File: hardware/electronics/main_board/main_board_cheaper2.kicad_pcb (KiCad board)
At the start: 2 copper layers, 125.5 x 125.5 mm, 144 parts, among them J1 TF-15X15, J2 RJ45, J3 Conn_02x04_Odd_Even, Q1 CSD18537NQ5A, Q2 CSD18537NQ5A, Q3 CSD18537NQ5A, Q4 CSD18537NQ5A, Q5 CSD18537NQ5A, Q6 CSD18537NQ5A, Q7 CSD18537NQ5A, Q8 CSD18537NQ5A, U1 P82B96

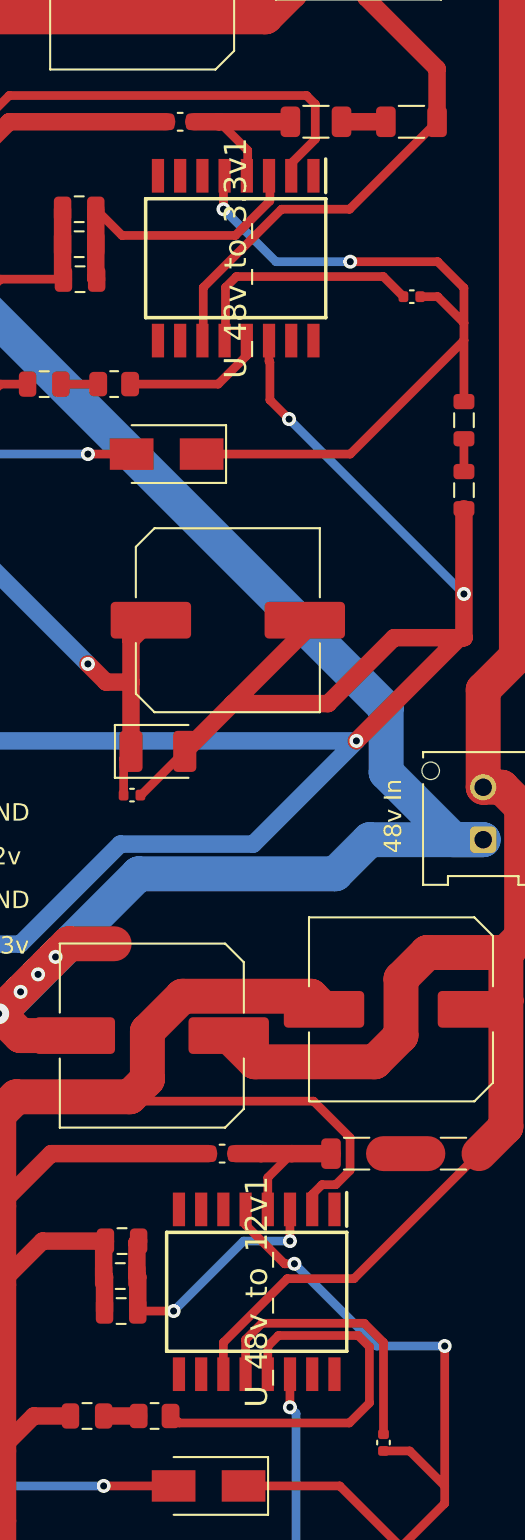
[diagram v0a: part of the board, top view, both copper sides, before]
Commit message: updated footprint to generic SOIC-16w so tooling rotates it properly."
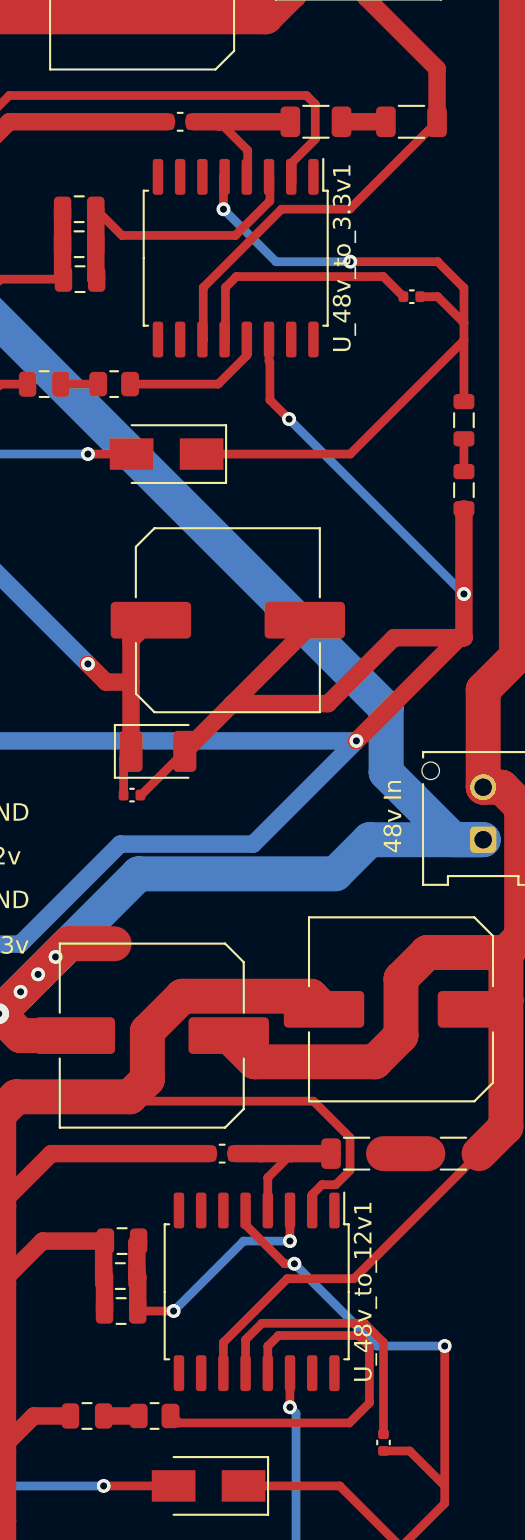
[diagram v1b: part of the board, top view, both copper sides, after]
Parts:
- U_48v_to_12v1, U_48v_to_3.3v1: footprint main_board:SOIC127P1032X265-16N -> Package_SO:SOIC-16W_7.5x10.3mm_P1.27mm

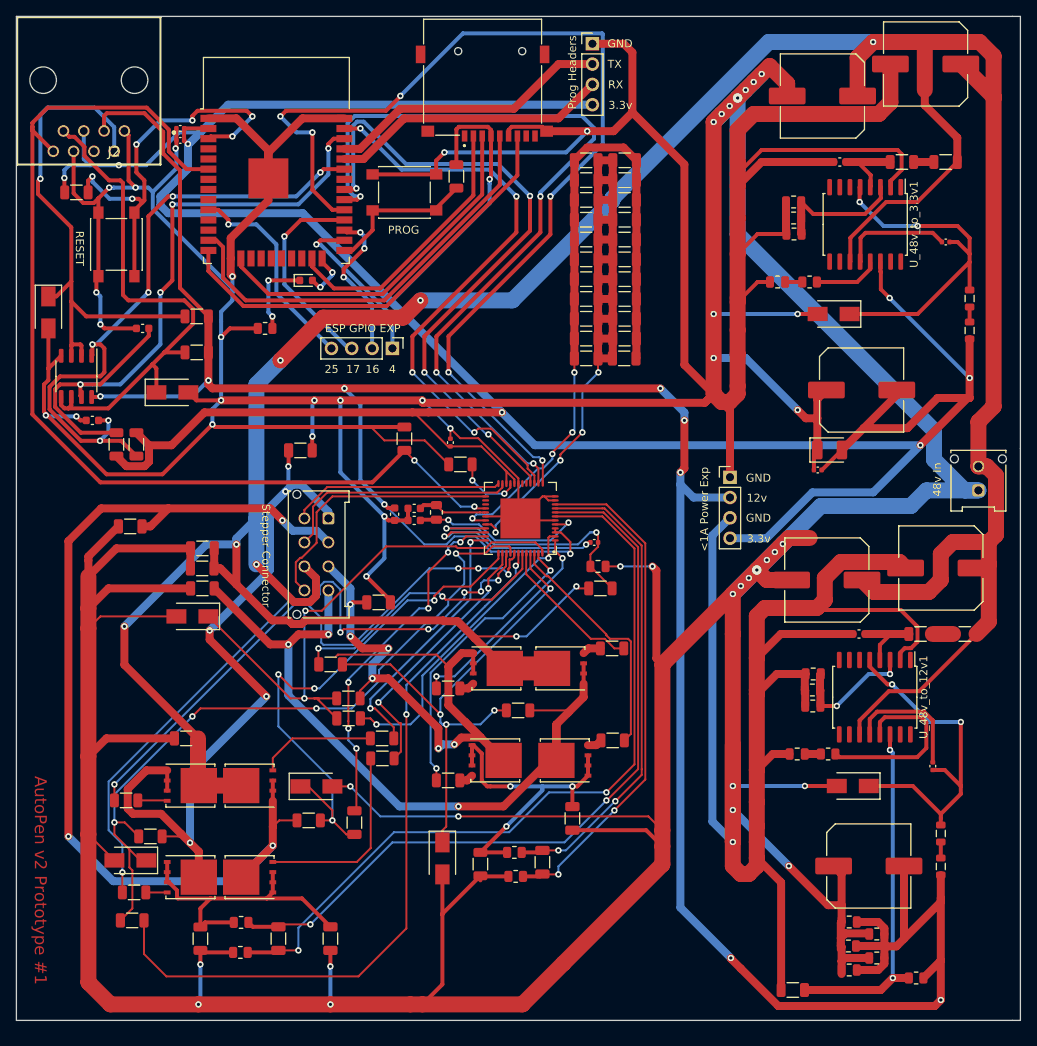
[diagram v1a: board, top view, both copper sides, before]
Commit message: added power split pcb
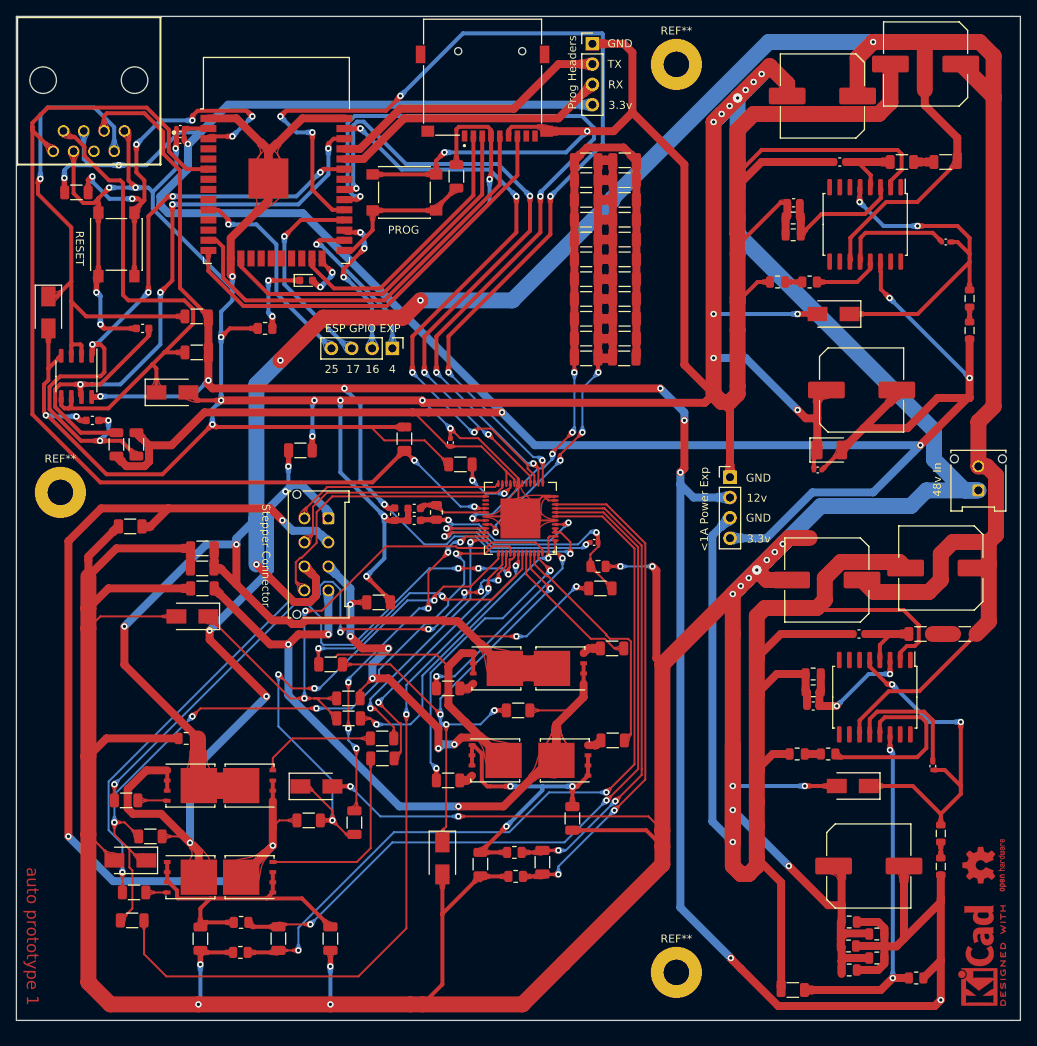
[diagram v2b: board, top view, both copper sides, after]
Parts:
- added REF**: OSHW-Logo2_7.3x6mm_Copper, Symbol:OSHW-Logo2_7.3x6mm_Copper, F.Cu at (134.0, 120.1)
- added REF**: KiCad-Logo2_5mm_Copper, Symbol:KiCad-Logo2_5mm_Copper, F.Cu at (133.7, 131.4)
- added REF**: MountingHole_3.2mm_M3_Pad, MountingHole:MountingHole_3.2mm_M3_Pad, F.Cu at (18.5, 73.5)
- added REF**: MountingHole_3.2mm_M3_Pad, MountingHole:MountingHole_3.2mm_M3_Pad, F.Cu at (95.5, 133.5)
- added REF**: MountingHole_3.2mm_M3_Pad, MountingHole:MountingHole_3.2mm_M3_Pad, F.Cu at (95.5, 20.0)
- C_12v_7, C_3.3v_8: footprint Capacitor_SMD:C_0805_2012Metric -> Capacitor_SMD:C_0603_1608Metric
- C_TMC_26: footprint Capacitor_SMD:C_1206_3216Metric -> Capacitor_SMD:C_0805_2012Metric
- moved C_3.3v_6 0.14 mm to (110.1, 41.3)
- moved C_12v_6 0.14 mm to (112.6, 98.3)
- moved C_3.3v_8 0.10 mm to (110.2, 37.3)
- moved C_3.3v_7 0.05 mm to (110.1, 39.2)
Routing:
- net 12v_comp_cap2: track 1432.3 -> 1435.2 mm
- net 3.3v_comp_cap3: track 16.9 -> 17.4 mm
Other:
- board text added: "auto prototype 1"
- board text removed: "AutoPen v2 Prototype #1"
